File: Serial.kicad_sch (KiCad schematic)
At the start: 19 parts

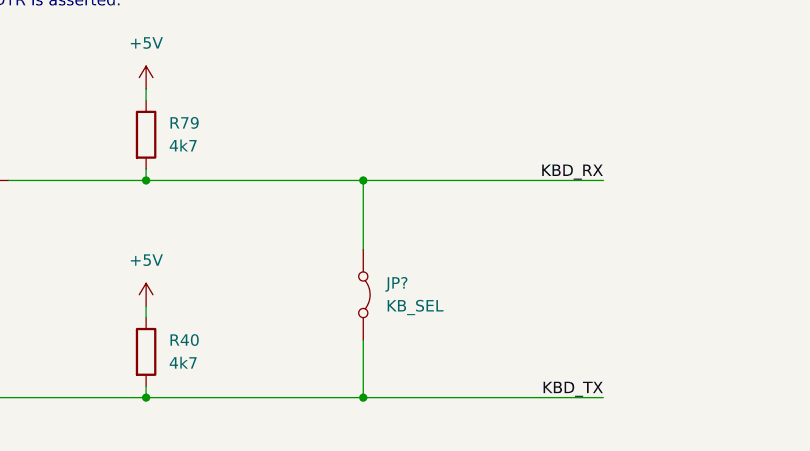
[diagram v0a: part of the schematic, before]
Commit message: Annotated all components
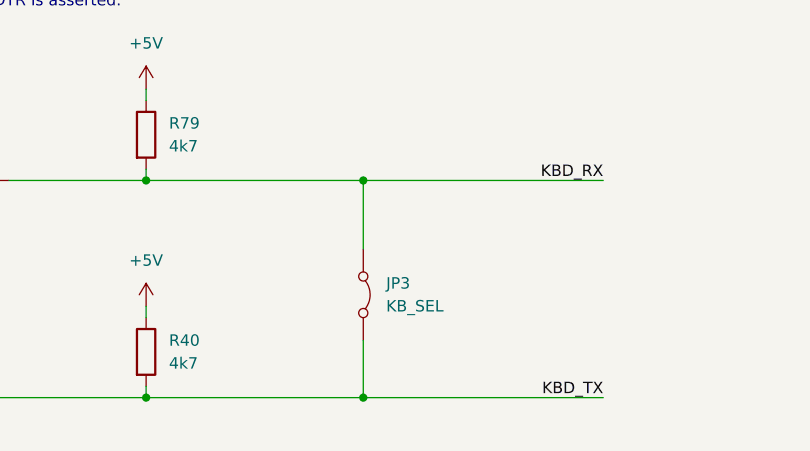
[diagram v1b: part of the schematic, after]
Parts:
- gave numbers to parts that had none: 2
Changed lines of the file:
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@@
 		(dnp no)
 		(fields_autoplaced yes)
-		(property "Reference" "J?"
+		(property "Reference" "J5"
 			(at 270.51 54.61 0)
 			(effects
@@
 			(project "ceda"
 				(path "/12a6dbe3-008d-4c5b-88f6-9f1c816060be/e6a0e8fd-e32c-428e-9a73-cac8f5494d05"
-					(reference "J?")
+					(reference "J5")
 					(unit 1)
 				)
@@
 		(dnp no)
 		(fields_autoplaced yes)
-		(property "Reference" "JP?"
+		(property "Reference" "JP3"
 			(at 118.11 171.4499 90)
 			(effects
@@
 			(project "ceda"
 				(path "/12a6dbe3-008d-4c5b-88f6-9f1c816060be/e6a0e8fd-e32c-428e-9a73-cac8f5494d05"
-					(reference "JP?")
+					(reference "JP3")
 					(unit 1)
 				)

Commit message: Assigned default footprints to ICs
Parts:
- UA15, UB9, UC15, UC2, UD14, UD15, UD16: footprint (none) -> Package_DIP:DIP-14_W7.62mm
- UC10: footprint (none) -> Package_DIP:DIP-40_W15.24mm
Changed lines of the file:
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@@
 			)
 		)
-		(property "Footprint" ""
+		(property "Footprint" "Package_DIP:DIP-14_W7.62mm"
 			(at 54.61 184.15 0)
 			(effects
@@
 			)
 		)
-		(property "Footprint" ""
+		(property "Footprint" "Package_DIP:DIP-14_W7.62mm"
 			(at 175.26 99.06 0)
 			(effects
@@
 			)
 		)
-		(property "Footprint" ""
+		(property "Footprint" "Package_DIP:DIP-14_W7.62mm"
 			(at 129.54 90.17 0)
 			(effects
@@
 			)
 		)
-		(property "Footprint" ""
+		(property "Footprint" "Package_DIP:DIP-14_W7.62mm"
 			(at 223.52 90.17 0)
 			(effects
@@
 			)
 		)
-		(property "Footprint" ""
+		(property "Footprint" "Package_DIP:DIP-14_W7.62mm"
 			(at 223.52 74.93 0)
 			(effects
@@
 			)
 		)
-		(property "Footprint" ""
+		(property "Footprint" "Package_DIP:DIP-14_W7.62mm"
 			(at 247.65 161.29 0)
 			(effects
@@
 			)
 		)
-		(property "Footprint" ""
+		(property "Footprint" "Package_DIP:DIP-40_W15.24mm"
 			(at 52.705 55.245 0)
 			(effects
@@
 			)
 		)
-		(property "Footprint" ""
+		(property "Footprint" "Package_DIP:DIP-14_W7.62mm"
 			(at 175.26 67.31 0)
 			(effects
@@
 			)
 		)
-		(property "Footprint" ""
+		(property "Footprint" "Package_DIP:DIP-14_W7.62mm"
 			(at 175.26 83.82 0)
 			(effects
@@
 			)
 		)
-		(property "Footprint" ""
+		(property "Footprint" "Package_DIP:DIP-14_W7.62mm"
 			(at 220.98 67.31 0)
 			(effects
@@
 			)
 		)
-		(property "Footprint" ""
+		(property "Footprint" "Package_DIP:DIP-14_W7.62mm"
 			(at 129.54 74.93 0)
 			(effects
@@
 			)
 		)
-		(property "Footprint" ""
+		(property "Footprint" "Package_DIP:DIP-14_W7.62mm"
 			(at 265.43 90.17 0)
 			(effects
@@
 			)
 		)
-		(property "Footprint" ""
+		(property "Footprint" "Package_DIP:DIP-14_W7.62mm"
 			(at 229.87 152.4 0)
 			(effects
@@
 			)
 		)
-		(property "Footprint" ""
+		(property "Footprint" "Package_DIP:DIP-14_W7.62mm"
 			(at 208.28 154.94 0)
 			(effects
@@
 			)
 		)
-		(property "Footprint" ""
+		(property "Footprint" "Package_DIP:DIP-14_W7.62mm"
 			(at 254 134.62 0)
 			(effects
@@
 			)
 		)
-		(property "Footprint" ""
+		(property "Footprint" "Package_DIP:DIP-14_W7.62mm"
 			(at 208.28 133.35 0)
 			(effects
@@
 			)
 		)
-		(property "Footprint" ""
+		(property "Footprint" "Package_DIP:DIP-14_W7.62mm"
 			(at 44.45 160.02 0)
 			(effects
@@
 			)
 		)
-		(property "Footprint" ""
+		(property "Footprint" "Package_DIP:DIP-14_W7.62mm"
 			(at 68.58 160.02 0)
 			(effects
@@
 			)
 		)
-		(property "Footprint" ""
+		(property "Footprint" "Package_DIP:DIP-14_W7.62mm"
 			(at 129.54 58.42 0)
 			(effects

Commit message: pcb: added and placed almost all components
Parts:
- C10, C3, C4, C5, C6, C8, C9: footprint (none) -> Capacitor_THT:C_Disc_D4.3mm_W1.9mm_P5.00mm
- J5: footprint (none) -> Connector_PinHeader_2.54mm:PinHeader_2x03_P2.54mm_Vertical
- JP3: footprint (none) -> Connector_PinHeader_2.54mm:PinHeader_2x01_P2.54mm_Vertical
- R40, R79: footprint (none) -> Resistor_THT:R_Axial_DIN0204_L3.6mm_D1.6mm_P5.08mm_Vertical
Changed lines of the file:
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@@
 			)
 		)
-		(property "Footprint" ""
+		(property "Footprint" "Connector_PinHeader_2.54mm:PinHeader_2x03_P2.54mm_Vertical"
 			(at 267.97 66.04 0)
 			(effects
@@
 			)
 		)
-		(property "Footprint" ""
+		(property "Footprint" "Capacitor_THT:C_Disc_D4.3mm_W1.9mm_P5.00mm"
 			(at 203.2 126.0348 0)
 			(effects
@@
 			)
 		)
-		(property "Footprint" ""
+		(property "Footprint" "Capacitor_THT:C_Disc_D4.3mm_W1.9mm_P5.00mm"
 			(at 124.46 82.8548 0)
 			(effects
@@
 			)
 		)
-		(property "Footprint" ""
+		(property "Footprint" "Connector_PinHeader_2.54mm:PinHeader_2x01_P2.54mm_Vertical"
 			(at 115.57 172.72 0)
 			(effects
@@
 			)
 		)
-		(property "Footprint" ""
+		(property "Footprint" "Capacitor_THT:C_Disc_D4.3mm_W1.9mm_P5.00mm"
 			(at 218.44 67.6148 0)
 			(effects
@@
 			)
 		)
-		(property "Footprint" ""
+		(property "Footprint" "Resistor_THT:R_Axial_DIN0204_L3.6mm_D1.6mm_P5.08mm_Vertical"
 			(at 89.662 179.07 90)
 			(effects
@@
 			)
 		)
-		(property "Footprint" ""
+		(property "Footprint" "Capacitor_THT:C_Disc_D4.3mm_W1.9mm_P5.00mm"
 			(at 218.44 82.8548 0)
 			(effects
@@
 			)
 		)
-		(property "Footprint" ""
+		(property "Footprint" "Resistor_THT:R_Axial_DIN0204_L3.6mm_D1.6mm_P5.08mm_Vertical"
 			(at 89.662 154.94 90)
 			(effects
@@
 			)
 		)
-		(property "Footprint" ""
+		(property "Footprint" "Capacitor_THT:C_Disc_D4.3mm_W1.9mm_P5.00mm"
 			(at 124.46 51.1048 0)
 			(effects
@@
 			)
 		)
-		(property "Footprint" ""
+		(property "Footprint" "Capacitor_THT:C_Disc_D4.3mm_W1.9mm_P5.00mm"
 			(at 124.46 67.6148 0)
 			(effects
@@
 			)
 		)
-		(property "Footprint" ""
+		(property "Footprint" "Capacitor_THT:C_Disc_D4.3mm_W1.9mm_P5.00mm"
 			(at 248.92 127.3048 0)
 			(effects

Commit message: pcb: added all the connector, 99% routed
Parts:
- renumbered C6 to C18, C4 to C19, C10 to C29, C9 to C30, C8 to C31
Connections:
- net +5V: now also R79.2; no longer R79.1
- net KBD_RX: now also R79.1; no longer R79.2
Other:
- moved on the sheet: R79
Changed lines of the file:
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@@
 	(wire
 		(pts
-			(xy 142.24 160.02) (xy 115.57 160.02)
+			(xy 133.35 160.02) (xy 115.57 160.02)
 		)
 		(stroke
@@
 	(wire
 		(pts
-			(xy 115.57 184.15) (xy 142.24 184.15)
+			(xy 115.57 184.15) (xy 133.35 184.15)
 		)
 		(stroke
@@
 		)
 	)
-	(label "KBD_RX"
-		(at 142.24 160.02 180)
-		(effects
-			(font
-				(size 1.27 1.27)
-			)
-			(justify right bottom)
-		)
-	)
 	(label "RxCA'"
 		(at 256.54 60.96 0)
@@
 		)
 	)
-	(label "KBD_TX"
-		(at 142.24 184.15 180)
-		(effects
-			(font
-				(size 1.27 1.27)
-			)
-			(justify right bottom)
-		)
-	)
 	(label "RxDA"
 		(at 115.57 58.42 0)
@@
 		)
 	)
+	(global_label "KBD_TX"
+		(shape input)
+		(at 133.35 184.15 0)
+		(fields_autoplaced yes)
+		(effects
+			(font
+				(size 1.27 1.27)
+			)
+			(justify left)
+		)
+		(property "Intersheetrefs" "${INTERSHEET_REFS}"
+			(at 143.2899 184.15 0)
+			(effects
+				(font
+					(size 1.27 1.27)
+				)
+				(justify left)
+				(hide yes)
+			)
+		)
+	)
 	(global_label "~{IE_1}"
 		(shape output)
@@
 		)
 	)
+	(global_label "KBD_RX"
+		(shape input)
+		(at 133.35 160.02 0)
+		(fields_autoplaced yes)
+		(effects
+			(font
+				(size 1.27 1.27)
+			)
+			(justify left)
+		)
+		(property "Intersheetrefs" "${INTERSHEET_REFS}"
+			(at 143.5923 160.02 0)
+			(effects
+				(font
+					(size 1.27 1.27)
+				)
+				(justify left)
+				(hide yes)
+			)
+		)
+	)
 	(global_label "PRNT_3"
 		(shape input)
@@
 		(dnp no)
 		(fields_autoplaced yes)
-		(property "Reference" "C10"
+		(property "Reference" "C29"
 			(at 120.65 76.2 90)
 			(effects
@@
 			(project "ceda"
 				(path "/12a6dbe3-008d-4c5b-88f6-9f1c816060be/e6a0e8fd-e32c-428e-9a73-cac8f5494d05"
-					(reference "C10")
+					(reference "C29")
 					(unit 1)
 				)
@@
 		(dnp no)
 		(fields_autoplaced yes)
-		(property "Reference" "C6"
+		(property "Reference" "C18"
 			(at 214.63 76.2 90)
 			(effects
@@
 			(project "ceda"
 				(path "/12a6dbe3-008d-4c5b-88f6-9f1c816060be/e6a0e8fd-e32c-428e-9a73-cac8f5494d05"
-					(reference "C6")
+					(reference "C18")
 					(unit 1)
 				)
@@
 	(symbol
 		(lib_id "Device:R")
-		(at 91.44 154.94 0)
+		(at 91.44 154.94 180)
 		(unit 1)
 		(exclude_from_sim no)
@@
 					(size 1.27 1.27)
 				)
-				(justify left)
+				(justify right)
 			)
 		)
@@
 					(size 1.27 1.27)
 				)
-				(justify left)
+				(justify right)
 			)
 		)
 		(property "Footprint" "Resistor_THT:R_Axial_DIN0204_L3.6mm_D1.6mm_P5.08mm_Vertical"
-			(at 89.662 154.94 90)
+			(at 93.218 154.94 90)
 			(effects
 				(font
@@
 		(dnp no)
 		(fields_autoplaced yes)
-		(property "Reference" "C8"
+		(property "Reference" "C31"
 			(at 120.65 44.45 90)
 			(effects
@@
 			(project "ceda"
 				(path "/12a6dbe3-008d-4c5b-88f6-9f1c816060be/e6a0e8fd-e32c-428e-9a73-cac8f5494d05"
-					(reference "C8")
+					(reference "C31")
 					(unit 1)
 				)
@@
 		(dnp no)
 		(fields_autoplaced yes)
-		(property "Reference" "C9"
+		(property "Reference" "C30"
 			(at 120.65 60.96 90)
 			(effects
@@
 			(project "ceda"
 				(path "/12a6dbe3-008d-4c5b-88f6-9f1c816060be/e6a0e8fd-e32c-428e-9a73-cac8f5494d05"
-					(reference "C9")
+					(reference "C30")
 					(unit 1)
 				)
@@
 		(dnp no)
 		(fields_autoplaced yes)
-		(property "Reference" "C4"
+		(property "Reference" "C19"
 			(at 245.11 120.65 90)
 			(effects
@@
 			(project "ceda"
 				(path "/12a6dbe3-008d-4c5b-88f6-9f1c816060be/e6a0e8fd-e32c-428e-9a73-cac8f5494d05"
-					(reference "C4")
+					(reference "C19")
 					(unit 1)
 				)

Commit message: pcb and sch: finished routing and fixing connections
There are still some minor inconsistencies (/WR, /RD, one PRINTER
signal), some passives missing (decoupling caps, power stage), but the
schematic and the pcb should be more or less complete.
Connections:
- net RxCA: now also J5.2 (A0); no longer J5.1 (A0)
- net RxCA': now also J5.1 (A1); no longer J5.6 (A1)
- net SER_CLK: now also J5.5 (C1); no longer J5.4 (C1)
- net TxCA: now also J5.4 (B0), J5.6 (C0); no longer J5.2 (B0), J5.3 (C0)
- net TxCA': now also J5.3 (B1); no longer J5.5 (B1)

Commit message: pcb: fixed traces
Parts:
- added C28: 330p, Capacitor_THT:C_Disc_D4.3mm_W1.9mm_P5.00mm, symbol Device:C
- added unit 5 of UD15
- added unit 5 of UD16
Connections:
- net GND: now also C28.1, UD15.7 (GND), UD16.7 (GND)
- net at UC15.12: now also C28.2
- new net +12V: UD15.14 (VCC+), UD16.14 (VCC+)
- new net -12V: UD15.1 (VCC-), UD16.1 (VCC-)
- no-connect marks 7 -> 6

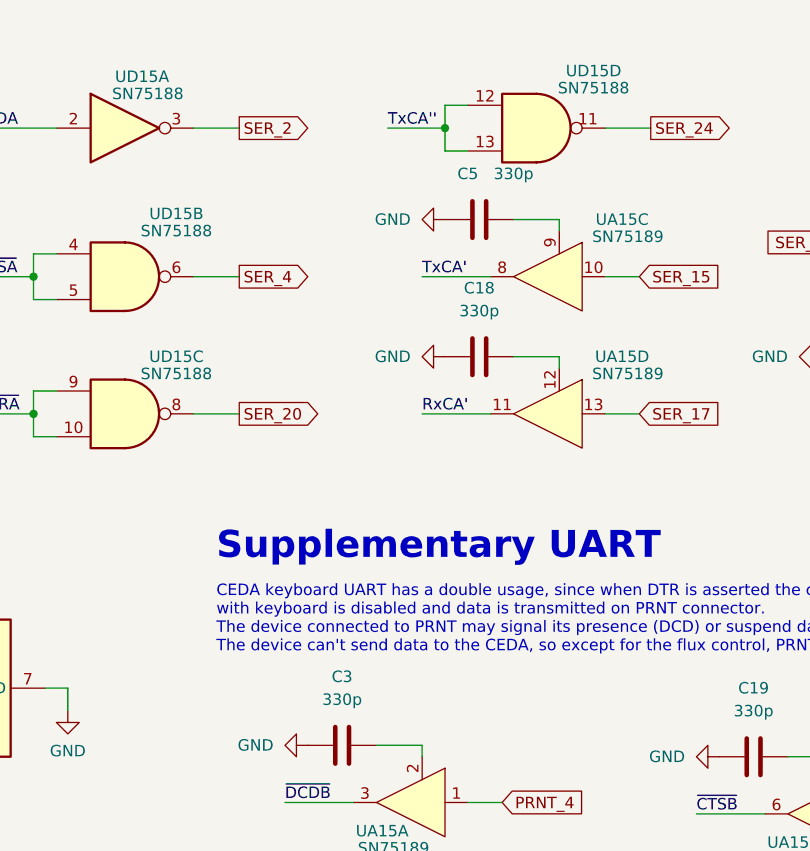
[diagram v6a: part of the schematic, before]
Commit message: pcb: added power in caps, reordered ref no, fixed power traces
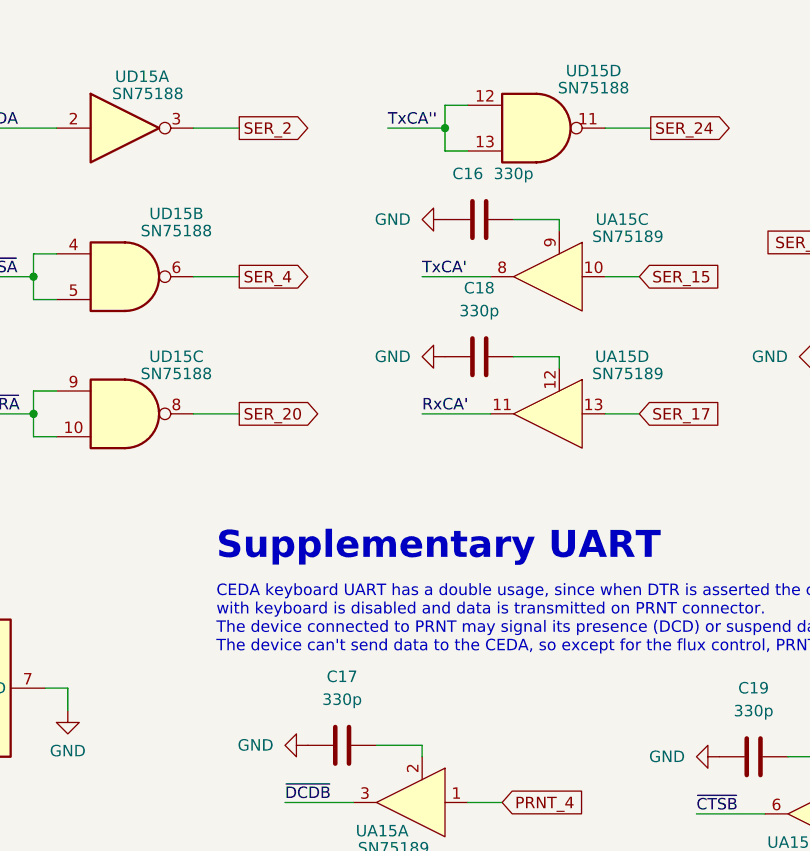
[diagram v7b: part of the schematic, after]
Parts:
- renumbered C5 to C16, C3 to C17
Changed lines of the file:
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@@
 		(dnp no)
 		(fields_autoplaced yes)
-		(property "Reference" "C3"
+		(property "Reference" "C17"
 			(at 199.39 119.38 90)
 			(effects
@@
 			(project "ceda"
 				(path "/12a6dbe3-008d-4c5b-88f6-9f1c816060be/e6a0e8fd-e32c-428e-9a73-cac8f5494d05"
-					(reference "C3")
+					(reference "C17")
 					(unit 1)
 				)
@@
 		(on_board yes)
 		(dnp no)
-		(property "Reference" "C5"
+		(property "Reference" "C16"
 			(at 213.36 63.5 90)
 			(effects
@@
 			(project "ceda"
 				(path "/12a6dbe3-008d-4c5b-88f6-9f1c816060be/e6a0e8fd-e32c-428e-9a73-cac8f5494d05"
-					(reference "C5")
+					(reference "C16")
 					(unit 1)
 				)
